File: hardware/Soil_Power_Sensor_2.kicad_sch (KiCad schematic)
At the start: 20 parts, among them J9 Conn_01x03_Pin, U5 REF2033, U8 TPS60400DBV

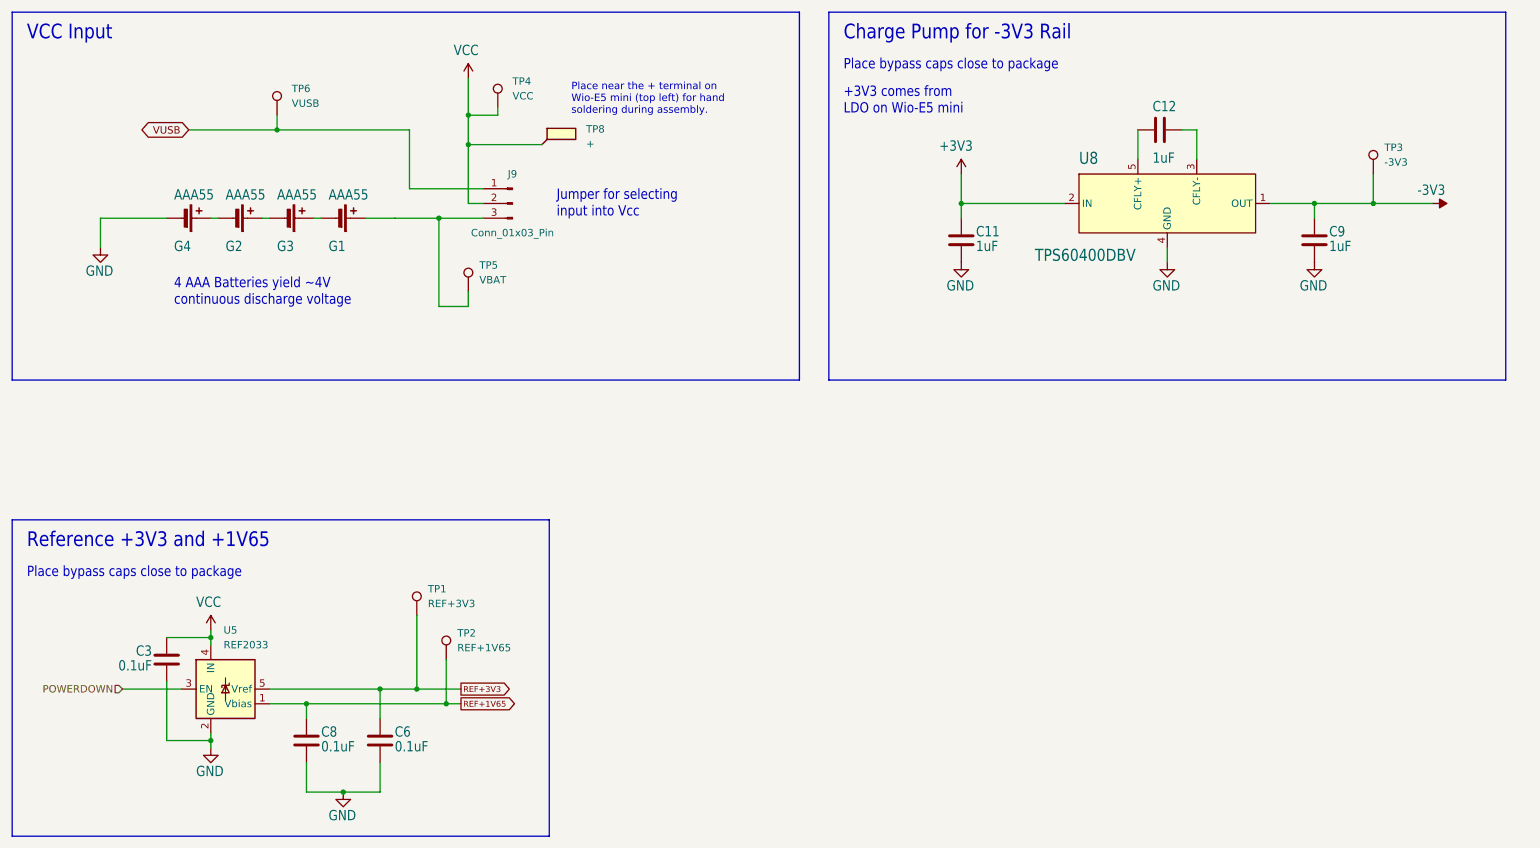
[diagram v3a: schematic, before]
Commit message: Updated annotations based on PCB position
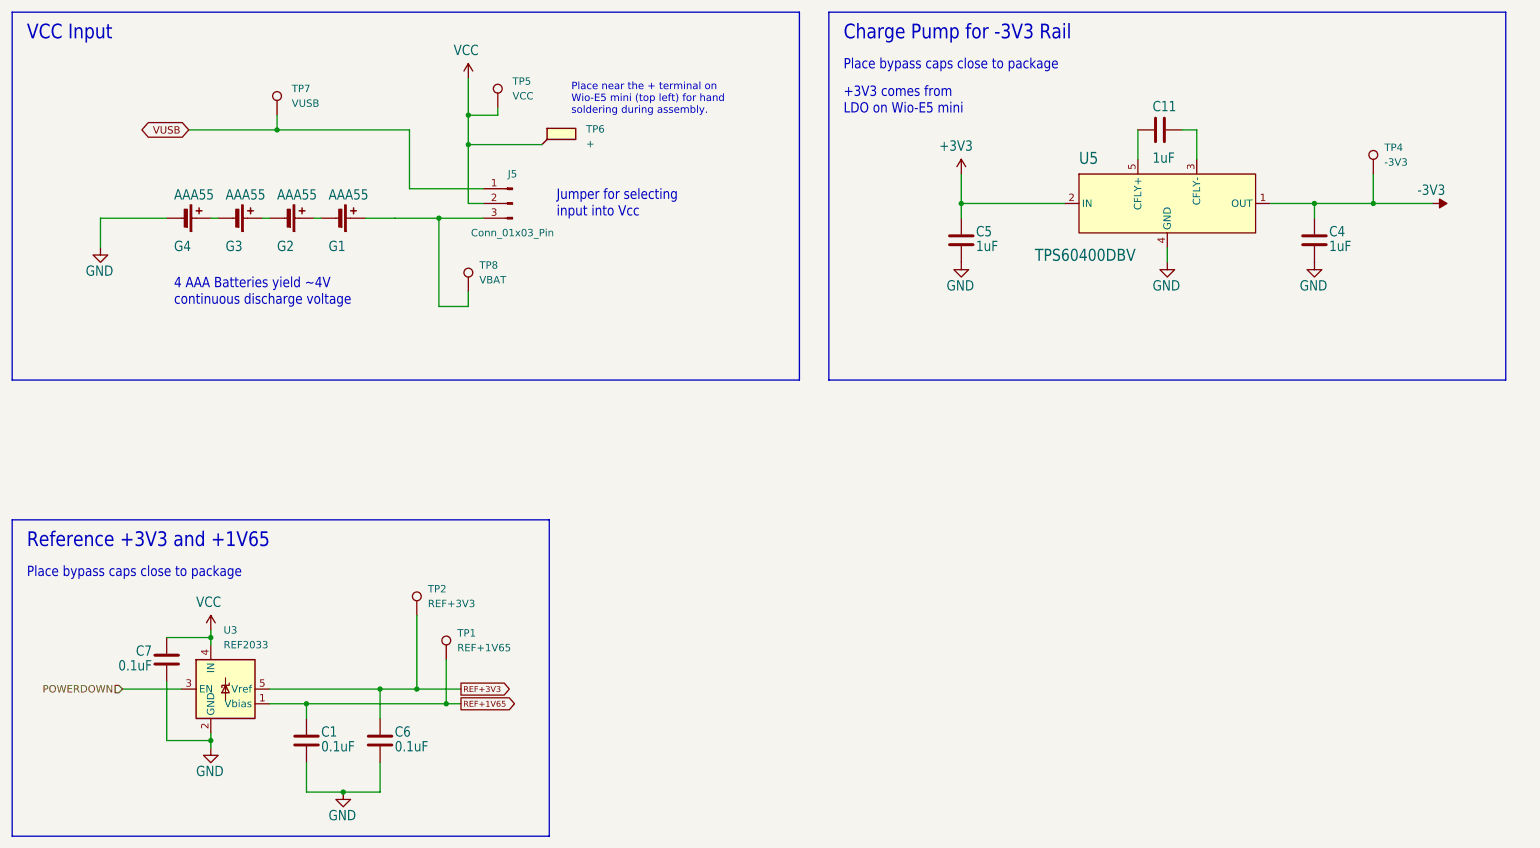
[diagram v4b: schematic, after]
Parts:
- renumbered C8 to C1, C12 to C11, C9 to C4, C11 to C5, C3 to C7, G3 to G2, G2 to G3, J9 to J5, TP2 to TP1, TP1 to TP2, TP3 to TP4, TP4 to TP5, TP8 to TP6, TP6 to TP7, TP5 to TP8, U5 to U3, U8 to U5
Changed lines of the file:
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@@
   (title_block
     (title "Soil Power Sensor")
-    (date "2023-10-09")
-    (rev "2.1.0")
+    (date "2024-03-08")
+    (rev "2.2.0")
     (company "jlab")
   )
@@
   (symbol (lib_id "Device:C") (at 184.15 59.69 0) (unit 1)
     (in_bom yes) (on_board yes) (dnp no)
-    (property "Reference" "C11" (at 186.69 57.15 0)
+    (property "Reference" "C5" (at 186.69 57.15 0)
       (effects (font (size 1.778 1.5113)) (justify left top))
     )
@@
       (project "Soil Power Sensor"
         (path "/5300ec4d-4648-40a1-8d89-4fa6b3bf32a3/642281e5-1644-4dc3-b6e5-bcf5b1c03ff1"
-          (reference "C11") (unit 1)
+          (reference "C5") (unit 1)
         )
       )
@@
   (symbol (lib_id "Reference_Voltage:REF2033") (at 57.15 137.16 0) (unit 1)
     (in_bom yes) (on_board yes) (dnp no) (fields_autoplaced)
-    (property "Reference" "U5" (at 56.8041 127 0)
+    (property "Reference" "U3" (at 56.8041 127 0)
       (effects (font (size 1.27 1.27)) (justify left))
     )
@@
       (project "Soil Power Sensor"
         (path "/5300ec4d-4648-40a1-8d89-4fa6b3bf32a3/642281e5-1644-4dc3-b6e5-bcf5b1c03ff1"
-          (reference "U5") (unit 1)
+          (reference "U3") (unit 1)
         )
       )
@@
   (symbol (lib_id "Soil Power Sensor-eagle-import:TPS60400DBV") (at 219.71 53.34 0) (unit 1)
     (in_bom yes) (on_board yes) (dnp no)
-    (property "Reference" "U8" (at 204.47 46.7614 0)
+    (property "Reference" "U5" (at 204.47 46.7614 0)
       (effects (font (size 2.0828 1.7703)) (justify left bottom))
     )
@@
       (project "Soil Power Sensor"
         (path "/5300ec4d-4648-40a1-8d89-4fa6b3bf32a3/642281e5-1644-4dc3-b6e5-bcf5b1c03ff1"
-          (reference "U8") (unit 1)
+          (reference "U5") (unit 1)
         )
       )
@@
   (symbol (lib_id "Connector:Conn_01x03_Pin") (at 106.68 53.34 0) (mirror y) (unit 1)
     (in_bom yes) (on_board yes) (dnp no)
-    (property "Reference" "J9" (at 106.68 48.26 0)
+    (property "Reference" "J5" (at 106.68 48.26 0)
       (effects (font (size 1.27 1.27)))
     )
@@
       (project "Soil Power Sensor"
         (path "/5300ec4d-4648-40a1-8d89-4fa6b3bf32a3/642281e5-1644-4dc3-b6e5-bcf5b1c03ff1"
-          (reference "J9") (unit 1)
+          (reference "J5") (unit 1)
         )
       )
@@
   (symbol (lib_id "Device:C") (at 46.99 132.08 180) (unit 1)
     (in_bom yes) (on_board yes) (dnp no)
-    (property "Reference" "C3" (at 44.45 129.54 0)
+    (property "Reference" "C7" (at 44.45 129.54 0)
       (effects (font (size 1.778 1.5113)) (justify left bottom))
     )
@@
       (project "Soil Power Sensor"
         (path "/5300ec4d-4648-40a1-8d89-4fa6b3bf32a3/642281e5-1644-4dc3-b6e5-bcf5b1c03ff1"
-          (reference "C3") (unit 1)
+          (reference "C7") (unit 1)
         )
       )
@@
   (symbol (lib_id "Device:Battery_Cell") (at 58.42 55.88 270) (mirror x) (unit 1)
     (in_bom yes) (on_board yes) (dnp no)
-    (property "Reference" "G2" (at 57.15 59.69 90)
+    (property "Reference" "G3" (at 57.15 59.69 90)
       (effects (font (size 1.778 1.5113)) (justify left bottom))
     )
@@
       (project "Soil Power Sensor"
         (path "/5300ec4d-4648-40a1-8d89-4fa6b3bf32a3/642281e5-1644-4dc3-b6e5-bcf5b1c03ff1"
-          (reference "G2") (unit 1)
+          (reference "G3") (unit 1)
         )
       )
@@
   (symbol (lib_id "Connector:TestPoint") (at 104.14 36.83 0) (unit 1)
     (in_bom yes) (on_board yes) (dnp no) (fields_autoplaced)
-    (property "Reference" "TP4" (at 106.68 32.258 0)
+    (property "Reference" "TP5" (at 106.68 32.258 0)
       (effects (font (size 1.27 1.27)) (justify left))
     )
@@
       (project "Soil Power Sensor"
         (path "/5300ec4d-4648-40a1-8d89-4fa6b3bf32a3/642281e5-1644-4dc3-b6e5-bcf5b1c03ff1"
-          (reference "TP4") (unit 1)
+          (reference "TP5") (unit 1)
         )
       )
@@
   (symbol (lib_id "Device:C") (at 71.12 146.05 0) (unit 1)
     (in_bom yes) (on_board yes) (dnp no)
-    (property "Reference" "C8" (at 73.66 143.51 0)
+    (property "Reference" "C1" (at 73.66 143.51 0)
       (effects (font (size 1.778 1.5113)) (justify left top))
     )
@@
       (project "Soil Power Sensor"
         (path "/5300ec4d-4648-40a1-8d89-4fa6b3bf32a3/642281e5-1644-4dc3-b6e5-bcf5b1c03ff1"
-          (reference "C8") (unit 1)
+          (reference "C1") (unit 1)
         )
       )
@@
   (symbol (lib_id "Connector:TestPoint") (at 66.04 38.1 0) (unit 1)
     (in_bom yes) (on_board yes) (dnp no) (fields_autoplaced)
-    (property "Reference" "TP6" (at 68.58 33.528 0)
+    (property "Reference" "TP7" (at 68.58 33.528 0)
       (effects (font (size 1.27 1.27)) (justify left))
     )
@@
       (project "Soil Power Sensor"
         (path "/5300ec4d-4648-40a1-8d89-4fa6b3bf32a3/642281e5-1644-4dc3-b6e5-bcf5b1c03ff1"
-          (reference "TP6") (unit 1)
+          (reference "TP7") (unit 1)
         )
       )
@@
   (symbol (lib_id "Connector:TestPoint") (at 95.25 132.08 0) (unit 1)
     (in_bom yes) (on_board yes) (dnp no) (fields_autoplaced)
-    (property "Reference" "TP2" (at 97.155 127.508 0)
+    (property "Reference" "TP1" (at 97.155 127.508 0)
       (effects (font (size 1.27 1.27)) (justify left))
     )
@@
       (project "Soil Power Sensor"
         (path "/5300ec4d-4648-40a1-8d89-4fa6b3bf32a3/642281e5-1644-4dc3-b6e5-bcf5b1c03ff1"
-          (reference "TP2") (unit 1)
+          (reference "TP1") (unit 1)
         )
       )
@@
   (symbol (lib_id "Device:C") (at 218.44 40.64 90) (unit 1)
     (in_bom yes) (on_board yes) (dnp no)
-    (property "Reference" "C12" (at 217.17 35.56 90)
+    (property "Reference" "C11" (at 217.17 35.56 90)
       (effects (font (size 1.778 1.5113)) (justify right bottom))
     )
@@
       (project "Soil Power Sensor"
         (path "/5300ec4d-4648-40a1-8d89-4fa6b3bf32a3/642281e5-1644-4dc3-b6e5-bcf5b1c03ff1"
-          (reference "C12") (unit 1)
+          (reference "C11") (unit 1)
         )
       )
@@
   (symbol (lib_id "Connector:TestPoint") (at 255.27 48.26 0) (unit 1)
     (in_bom yes) (on_board yes) (dnp no) (fields_autoplaced)
-    (property "Reference" "TP3" (at 257.175 43.688 0)
+    (property "Reference" "TP4" (at 257.175 43.688 0)
       (effects (font (size 1.27 1.27)) (justify left))
     )
@@
       (project "Soil Power Sensor"
         (path "/5300ec4d-4648-40a1-8d89-4fa6b3bf32a3/642281e5-1644-4dc3-b6e5-bcf5b1c03ff1"
-          (reference "TP3") (unit 1)
+          (reference "TP4") (unit 1)
         )
       )
@@
   (symbol (lib_id "Connector:TestPoint") (at 90.17 124.46 0) (unit 1)
     (in_bom yes) (on_board yes) (dnp no) (fields_autoplaced)
-    (property "Reference" "TP1" (at 92.075 119.888 0)
+    (property "Reference" "TP2" (at 92.075 119.888 0)
       (effects (font (size 1.27 1.27)) (justify left))
     )
@@
       (project "Soil Power Sensor"
         (path "/5300ec4d-4648-40a1-8d89-4fa6b3bf32a3/642281e5-1644-4dc3-b6e5-bcf5b1c03ff1"
-          (reference "TP1") (unit 1)
+          (reference "TP2") (unit 1)
         )
       )
@@
   (symbol (lib_id "Device:C") (at 245.11 59.69 0) (unit 1)
     (in_bom yes) (on_board yes) (dnp no)
-    (property "Reference" "C9" (at 247.65 57.15 0)
+    (property "Reference" "C4" (at 247.65 57.15 0)
       (effects (font (size 1.778 1.5113)) (justify left top))
     )
@@
       (project "Soil Power Sensor"
         (path "/5300ec4d-4648-40a1-8d89-4fa6b3bf32a3/642281e5-1644-4dc3-b6e5-bcf5b1c03ff1"
-          (reference "C9") (unit 1)
+          (reference "C4") (unit 1)
         )
       )
@@
   (symbol (lib_id "Device:Battery_Cell") (at 67.31 55.88 270) (mirror x) (unit 1)
     (in_bom yes) (on_board yes) (dnp no)
-    (property "Reference" "G3" (at 66.04 59.69 90)
+    (property "Reference" "G2" (at 66.04 59.69 90)
       (effects (font (size 1.778 1.5113)) (justify left bottom))
     )
@@
       (project "Soil Power Sensor"
         (path "/5300ec4d-4648-40a1-8d89-4fa6b3bf32a3/642281e5-1644-4dc3-b6e5-bcf5b1c03ff1"
-          (reference "G3") (unit 1)
+          (reference "G2") (unit 1)
         )
       )
@@
   (symbol (lib_id "Connector:TestPoint_Flag") (at 111.76 43.18 0) (unit 1)
     (in_bom yes) (on_board yes) (dnp no) (fields_autoplaced)
-    (property "Reference" "TP8" (at 119.38 40.513 0)
+    (property "Reference" "TP6" (at 119.38 40.513 0)
       (effects (font (size 1.27 1.27)) (justify left))
     )
@@
       (project "Soil Power Sensor"
         (path "/5300ec4d-4648-40a1-8d89-4fa6b3bf32a3/642281e5-1644-4dc3-b6e5-bcf5b1c03ff1"
-          (reference "TP8") (unit 1)
+          (reference "TP6") (unit 1)
         )
       )
@@
   (symbol (lib_id "Connector:TestPoint") (at 99.06 68.58 0) (unit 1)
     (in_bom yes) (on_board yes) (dnp no) (fields_autoplaced)
-    (property "Reference" "TP5" (at 100.965 64.008 0)
+    (property "Reference" "TP8" (at 100.965 64.008 0)
       (effects (font (size 1.27 1.27)) (justify left))
     )
@@
       (project "Soil Power Sensor"
         (path "/5300ec4d-4648-40a1-8d89-4fa6b3bf32a3/642281e5-1644-4dc3-b6e5-bcf5b1c03ff1"
-          (reference "TP5") (unit 1)
-        )
-      )
+          (reference "TP8") (unit 1)
+        )
+      )
